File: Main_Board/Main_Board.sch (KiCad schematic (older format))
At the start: 2 parts

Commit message: Started Main Board
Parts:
- added D?: D_Zener, symbol Device:D_Zener
- added J?: 12V_REG_IN, symbol Connector:Screw_Terminal_01x02
- added J?: 12V_REG_OUT, symbol Connector:Screw_Terminal_01x02
- added J?: Conn_02x08_Row_Letter_First, symbol Connector_Generic:Conn_02x08_Row_Letter_First
- added J?: BATT_IN, AMASS_XT60-M, symbol XT60-M:XT60-M
- added Q?: Q_PMOS_GDS, symbol Device:Q_PMOS_GDS
- added R?: R, symbol Device:R
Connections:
- net GND: now also J?.1 (-), J?.2 (Pin_2), J?.2 (Pin_2), R?.2
- net at U?.10 (CS1): no longer U?.10 (CS1)
- net at U?.11 (MOSI): no longer U?.11 (MOSI)
- net at U?.12 (MISO): no longer U?.12 (MISO)
- net at U?.13 (SCK): no longer U?.13 (SCK)
- new net: D?.1 (K), Q?.1 (G), R?.1
- new net: D?.2 (A), J?.1 (Pin_1), Q?.3 (S)
- new net +12V: J?.1 (Pin_1)
- new net +VDC: J?.2 (+), Q?.2 (D)
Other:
- moved on the sheet: U?

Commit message: Rounding up main and light board
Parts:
- removed J?: Conn_02x08_Row_Letter_First, symbol Connector_Generic:Conn_02x08_Row_Letter_First
- added C?: 0.1u, symbol Device:C
- added C?: 47u, symbol Device:C
- added C?: 10n, symbol Device:C_Small
- added C?: 6.8n, symbol Device:C_Small
- added C?: 22u, symbol Device:C
- added J?: Conn_02x07_Counter_Clockwise, symbol Connector_Generic:Conn_02x07_Counter_Clockwise
- added L?: 8.2u, symbol Device:L
- added Q?: Q_PMOS_GDS, symbol Device:Q_PMOS_GDS
- added R?: 100k, symbol Device:R
- added R?: 45.3k, symbol Device:R_Small
- added R? (x2): 10k, symbol Device:R_Small
- added R?: 6.8k, symbol Device:R_Small
- added U?: AP6503, symbol Regulator_Switching:AP6503
- J3: renamed from J?; footprint AMASS_XT60-M -> (none)
- U1, U2: renamed from U?; footprint MODULE_DEV-16771 -> Main_Board:TEENSY_4_1_FP
- gave numbers to parts that had none: 5
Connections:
- net +5V: now also U1.VIN, U2.VIN, C?.1, J?.1 (Pin_1), J?.2 (Pin_2), L?.2, R?.1; no longer U1.5V, U2.5V
- net +VDC: now also C?.1, Q?.3 (S), R?.1, U?.2 (IN); no longer J3.2 (+)
- net GND: now also C?.2, C?.2, C?.2, C?.2, J?.8 (Pin_8), J?.9 (Pin_9), R?.2, R?.2, U?.4 (GND), U?.9 (EP)
- net +3V3: now reaches U1.3.3V_1 (3.3V), U1.3.3V_2 (3.3V), U1.3.3V_3 (3.3V)
- new net: J3.2 (+), Q?.2 (D)
- new net: C?.1, U?.1 (BST)
- new net: C?.2, L?.1, U?.3 (SW)
- new net: R?.1, R?.2, U?.5 (FB)
- new net: R?.1, U?.6 (COMP)
- new net: R?.2, U?.7 (EN)
- new net: C?.1, U?.8 (SS)
- new net: C?.1, R?.2
- new net: Q?.1 (G), R?.1
- new net D: J?.13 (Pin_13)
- new net LIGHT_EN: J?.14 (Pin_14)
- new net P0: J?.3 (Pin_3)
- new net P1: J?.4 (Pin_4)
- new net P2: J?.5 (Pin_5)
- new net P3: J?.6 (Pin_6)
- new net P4: J?.7 (Pin_7)
- new net ~CS: J?.10 (Pin_10)
- new net ~EN: J?.12 (Pin_12)
- new net ~WR: J?.11 (Pin_11)
- no-connect marks 0 -> 2
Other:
- moved on the sheet: D1, J1, J2, J3, Q1, R1

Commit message: Stuff with light
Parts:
- J1: value 12V_REG_IN -> 12V_REG_OUT
- J2: value 12V_REG_OUT -> 12V_REG_IN
- U1: value TEENSY_4_1 -> TEENSY_4_1_MASTER
- U2: value TEENSY_4_1 -> TEENSY_4_1_SLAVE
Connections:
- net +12V: now also Q1.2 (D); no longer J2.1 (Pin_1)
- net +VDC: now also J2.1 (Pin_1); no longer Q1.2 (D)
- net at U1.10 (CS1): now also U2.10 (CS1)
- net at U1.11 (MOSI): now also U2.11 (MOSI)
- net at U1.12 (MISO): now also U2.12 (MISO)
- net SCK_MASTER: now reaches U1.13 (SCK)
- net SCK_MASTER: now also U2.13 (SCK)
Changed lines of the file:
@@
 $EndDescr
-$Comp
-L TEENSY_4_1:TEENSY_4_1 U2
-U 1 1 61B38CB8
-P 12550 7750
-F 0 "U2" H 12550 9917 50  0000 C CNN
-F 1 "TEENSY_4_1" H 12550 9826 50  0000 C CNN
-F 2 "Main_Board:TEENSY_4_1_FP" H 12550 7750 50  0001 L BNN
-F 3 "" H 12550 7750 50  0001 L BNN
-F 4 "Manufacturer recommendations" H 12550 7750 50  0001 L BNN "STANDARD"
-F 5 "4.07mm" H 12550 7750 50  0001 L BNN "MAXIMUM_PACKAGE_HEIGHT"
-F 6 "4.1" H 12550 7750 50  0001 L BNN "PARTREV"
-F 7 "SparkFun Electronics" H 12550 7750 50  0001 L BNN "MANUFACTURER"
-	1    12550 7750
-	-1   0    0    -1
-$EndComp
 $Comp
 L power:GND #PWR0101
@@
 P 10500 7750
 F 0 "U1" H 10500 9917 50  0000 C CNN
-F 1 "TEENSY_4_1" H 10500 9826 50  0000 C CNN
+F 1 "TEENSY_4_1_MASTER" H 10500 9826 50  0000 C CNN
 F 2 "Main_Board:TEENSY_4_1_FP" H 10500 7750 50  0001 L BNN
 F 3 "" H 10500 7750 50  0001 L BNN
@@
 L power:+VDC #PWR0103
 U 1 1 61C63404
-P 16400 6200
-F 0 "#PWR0103" H 16400 6100 50  0001 C CNN
-F 1 "+VDC" H 16400 6475 50  0000 C CNN
-F 2 "" H 16400 6200 50  0001 C CNN
-F 3 "" H 16400 6200 50  0001 C CNN
-	1    16400 6200
+P 17150 7200
+F 0 "#PWR0103" H 17150 7100 50  0001 C CNN
+F 1 "+VDC" H 17150 7475 50  0000 C CNN
+F 2 "" H 17150 7200 50  0001 C CNN
+F 3 "" H 17150 7200 50  0001 C CNN
+	1    17150 7200
 	1    0    0    -1
 $EndComp
@@
 P 16650 7250
 F 0 "J1" H 16600 6950 50  0000 L CNN
-F 1 "12V_REG_IN" H 16450 7050 50  0000 L CNN
+F 1 "12V_REG_OUT" H 16450 7050 50  0000 L CNN
 F 2 "" H 16650 7250 50  0001 C CNN
 F 3 "~" H 16650 7250 50  0001 C CNN
@@
 P 16900 7250
 F 0 "J2" H 16900 7450 50  0000 C CNN
-F 1 "12V_REG_OUT" H 16950 7350 50  0000 C CNN
+F 1 "12V_REG_IN" H 16950 7350 50  0000 C CNN
 F 2 "" H 16900 7250 50  0001 C CNN
 F 3 "~" H 16900 7250 50  0001 C CNN
@@
 L power:+12V #PWR0106
 U 1 1 61C6E3B5
-P 17150 7200
-F 0 "#PWR0106" H 17150 7050 50  0001 C CNN
-F 1 "+12V" H 17165 7373 50  0000 C CNN
-F 2 "" H 17150 7200 50  0001 C CNN
-F 3 "" H 17150 7200 50  0001 C CNN
-	1    17150 7200
+P 16400 6200
+F 0 "#PWR0106" H 16400 6050 50  0001 C CNN
+F 1 "+12V" H 16415 6373 50  0000 C CNN
+F 2 "" H 16400 6200 50  0001 C CNN
+F 3 "" H 16400 6200 50  0001 C CNN
+	1    16400 6200
 	1    0    0    -1
 $EndComp
@@
 Wire Wire Line
 	20050 9050 19950 9050
+Wire Wire Line
+	11300 8150 11750 8150
+Wire Wire Line
+	11300 8250 11750 8250
+Wire Wire Line
+	11300 7950 11750 7950
+$Comp
+L TEENSY_4_1:TEENSY_4_1 U2
+U 1 1 61B38CB8
+P 12550 7750
+F 0 "U2" H 12550 9917 50  0000 C CNN
+F 1 "TEENSY_4_1_SLAVE" H 12550 9826 50  0000 C CNN
+F 2 "Main_Board:TEENSY_4_1_FP" H 12550 7750 50  0001 L BNN
+F 3 "" H 12550 7750 50  0001 L BNN
+F 4 "Manufacturer recommendations" H 12550 7750 50  0001 L BNN "STANDARD"
+F 5 "4.07mm" H 12550 7750 50  0001 L BNN "MAXIMUM_PACKAGE_HEIGHT"
+F 6 "4.1" H 12550 7750 50  0001 L BNN "PARTREV"
+F 7 "SparkFun Electronics" H 12550 7750 50  0001 L BNN "MANUFACTURER"
+	1    12550 7750
+	-1   0    0    -1
+$EndComp
+Text GLabel 9600 8350 0    50   Output ~ 0
+SCK_MASTER
+Wire Wire Line
+	9600 8350 9700 8350
+Text GLabel 13500 8350 2    50   Input ~ 0
+SCK_MASTER
+Wire Wire Line
+	13500 8350 13350 8350
+$Comp
+L Graphic:SYM_Arrow_Small #SYM?
+U 1 1 61E13D0E
+P 11500 8250
+F 0 "#SYM?" H 11500 8310 50  0001 C CNN
+F 1 "SYM_Arrow_Small" H 11510 8200 50  0001 C CNN
+F 2 "" H 11500 8250 50  0001 C CNN
+F 3 "~" H 11500 8250 50  0001 C CNN
+	1    11500 8250
+	1    0    0    -1
+$EndComp
+$Comp
+L Graphic:SYM_Arrow_Small #SYM?
+U 1 1 61E15938
+P 11500 8150
+F 0 "#SYM?" H 11500 8210 50  0001 C CNN
+F 1 "SYM_Arrow_Small" H 11510 8100 50  0001 C CNN
+F 2 "" H 11500 8150 50  0001 C CNN
+F 3 "~" H 11500 8150 50  0001 C CNN
+	1    11500 8150
+	-1   0    0    1
+$EndComp
+$Comp
+L Graphic:SYM_Arrow_Small #SYM?
+U 1 1 61E1785A
+P 11500 7950
+F 0 "#SYM?" H 11500 8010 50  0001 C CNN
+F 1 "SYM_Arrow_Small" H 11510 7900 50  0001 C CNN
+F 2 "" H 11500 7950 50  0001 C CNN
+F 3 "~" H 11500 7950 50  0001 C CNN
+	1    11500 7950
+	1    0    0    -1
+$EndComp
 $EndSCHEMATC

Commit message: motor drivers added
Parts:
- added D? (x4): WS2812B, LED_SMD:LED_WS2812B_PLCC4_5.0x5.0mm_P3.2mm, symbol LED:WS2812B
- added J?: Conn_02x08_Row_Letter_First, symbol Connector_Generic:Conn_02x08_Row_Letter_First
- added R?: 10k, symbol Device:R
- added SW?: SW_Push, symbol Switch:SW_Push
- added SW?: SW_SPST, symbol Switch:SW_SPST
- added U? (x3): G2-24v13, symbol Main_Board:G2-24v13
- R1: value R -> 10k
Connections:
- net +3V3: now also J?.b1 (Pin_b1), SW?.2
- net +5V: now also D?.1 (VDD), D?.1 (VDD), D?.1 (VDD), D?.1 (VDD)
- net GND: now also D?.3 (VSS), D?.3 (VSS), D?.3 (VSS), D?.3 (VSS), J?.a1 (Pin_a1), R?.1, SW?.1 (A); no longer R?.2
- new net: R?.2, SW?.2 (B)
- new net: D?.2 (DOUT), D?.4 (DIN) (x4)
- new net HOLD_SW: R?.2, SW?.1
- new net IR1: J?.a8 (Pin_a8)
- new net IR10: J?.b6 (Pin_b6)
- new net IR11: J?.b5 (Pin_b5)
- new net IR12: J?.b4 (Pin_b4)
- new net IR13: J?.b3 (Pin_b3)
- new net IR14: J?.b2 (Pin_b2)
- new net IR2: J?.a7 (Pin_a7)
- new net IR3: J?.a6 (Pin_a6)
- new net IR4: J?.a5 (Pin_a5)
- new net IR5: J?.a4 (Pin_a4)
- new net IR6: J?.a3 (Pin_a3)
- new net IR7: J?.a2 (Pin_a2)
- new net IR8: J?.b8 (Pin_b8)
- new net IR9: J?.b7 (Pin_b7)
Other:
- moved on the sheet: C?, D1, J1, J2, J3, L?, Q1, Q?, R1, R?, U?

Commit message: changed document settings
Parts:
- added J? (x3): Conn_01x06, symbol Connector_Generic:Conn_01x06
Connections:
- net +12V: now also U?.4 (VIN), U?.4 (VIN), U?.4 (VIN)
- net GND: now also U?.1 (GND), U?.1 (GND), U?.1 (GND)
- net at U?.2 (OUTB): now also J?.1 (Pin_1) (x3)
- net at U?.3 (OUTA): now also J?.2 (Pin_2) (x3)
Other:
- moved on the sheet: C?, D1, D?, J1, J2, J3, J?, L?, Q1, Q?, R1, R?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

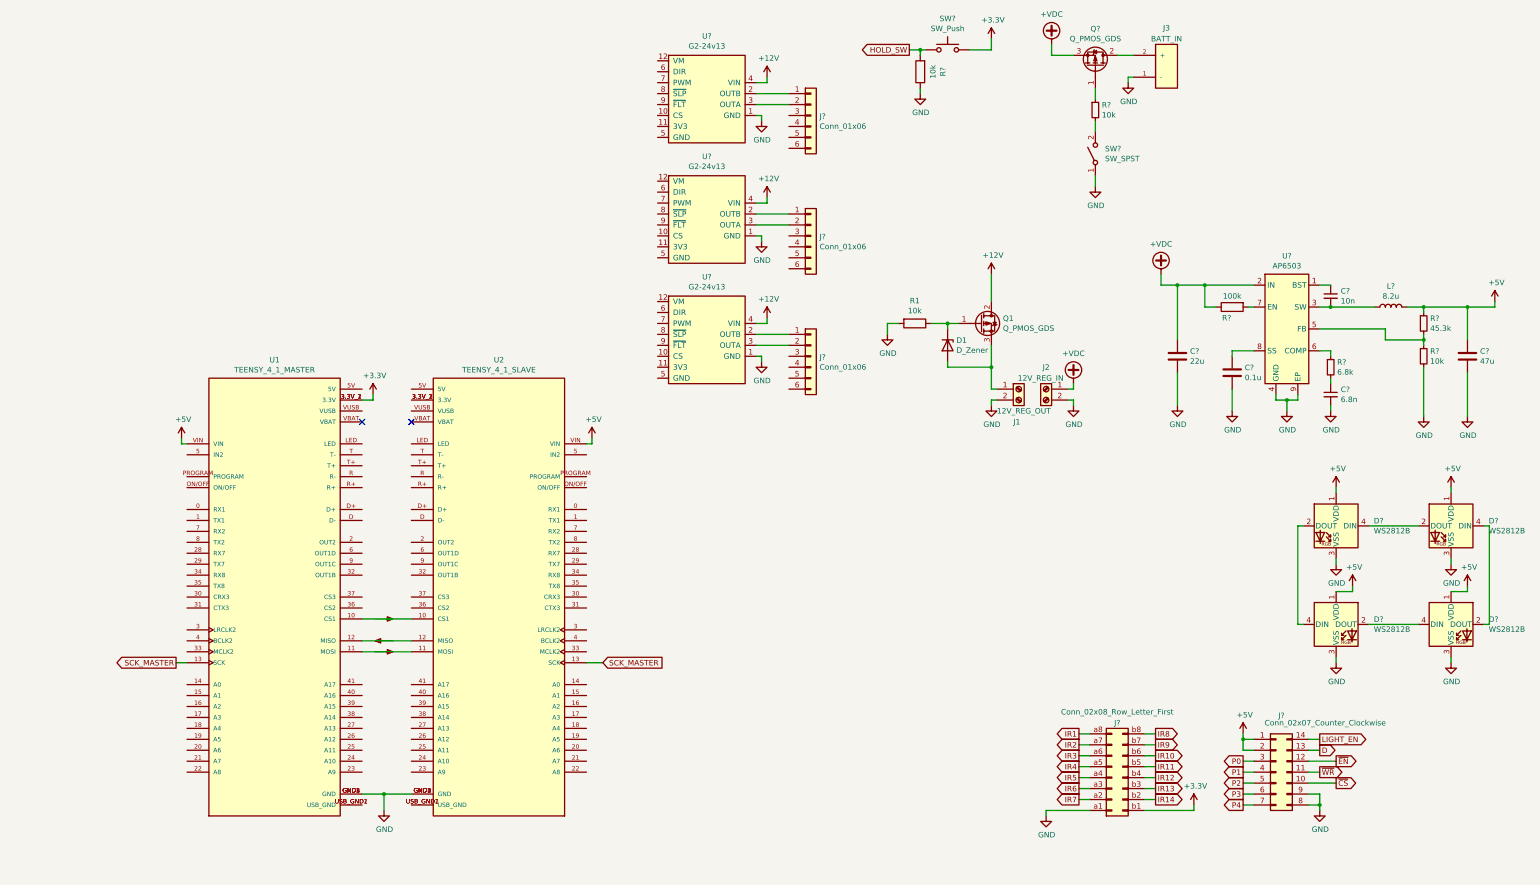
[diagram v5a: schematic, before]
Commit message: Added all connectors, layout for pins
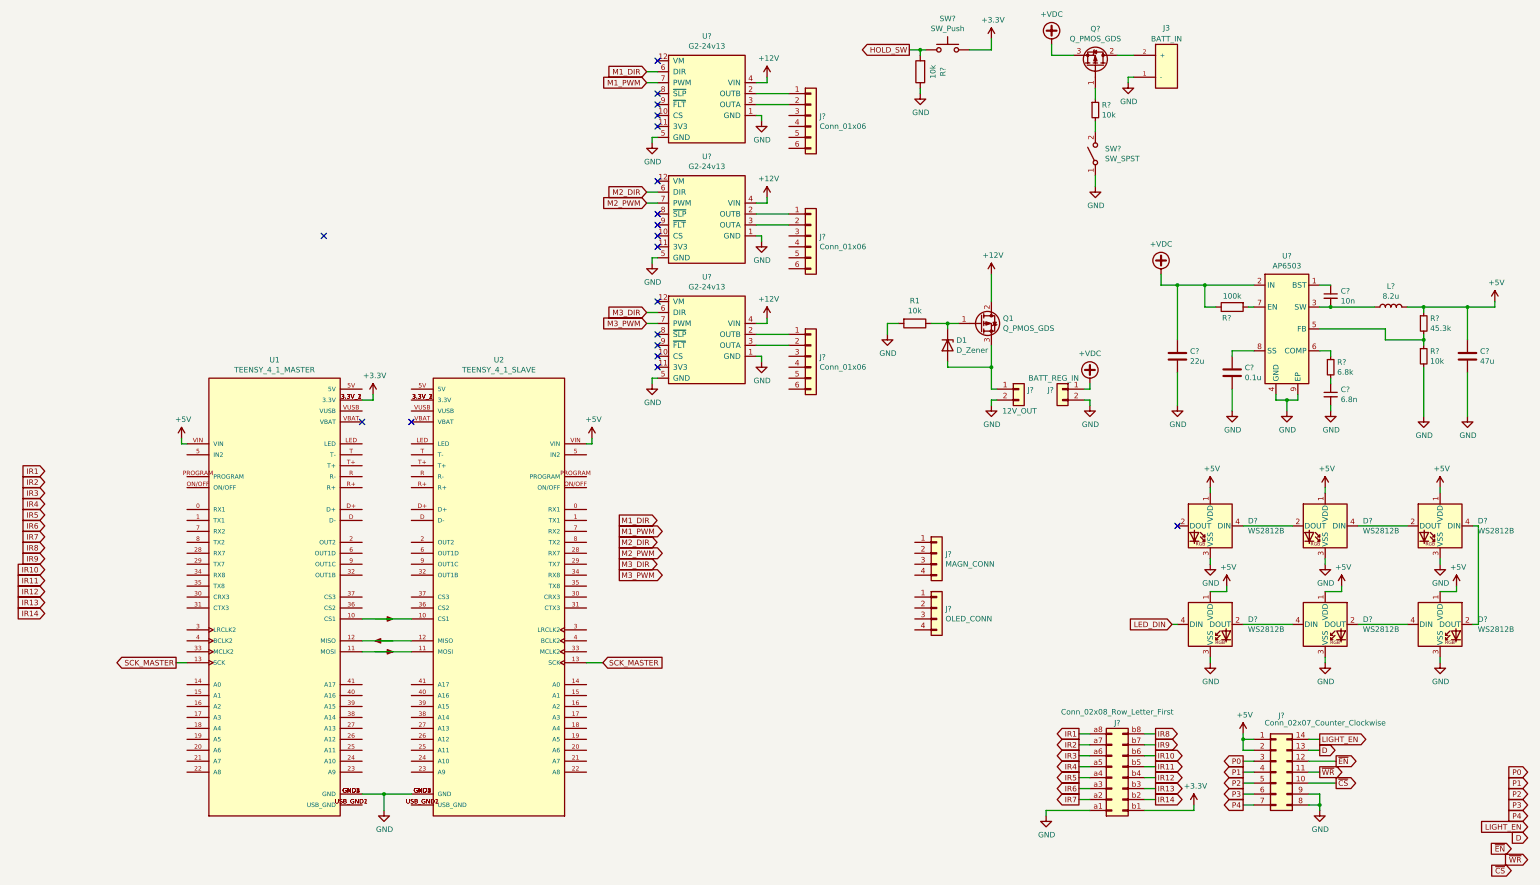
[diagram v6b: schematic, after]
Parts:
- removed J1: 12V_REG_OUT, symbol Connector:Screw_Terminal_01x02
- removed J2: 12V_REG_IN, symbol Connector:Screw_Terminal_01x02
- added D? (x2): WS2812B, LED_SMD:LED_WS2812B_PLCC4_5.0x5.0mm_P3.2mm, symbol LED:WS2812B
- added J?: MAGN_CONN, symbol Connector_Generic:Conn_01x04
- added J?: OLED_CONN, symbol Connector_Generic:Conn_01x04
- added J?: 12V_OUT, symbol Connector_Generic:Conn_01x02
- added J?: BATT_REG_IN, symbol Connector_Generic:Conn_01x02
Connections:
- net +5V: now also D?.1 (VDD), D?.1 (VDD)
- net +VDC: now also J?.1 (Pin_1)
- net GND: now also U?.5 (GND), U?.5 (GND), U?.5 (GND), D?.3 (VSS), D?.3 (VSS), J?.2 (Pin_2), J?.2 (Pin_2)
- net at D1.2 (A), Q1.3 (S): now also J?.1 (Pin_1)
- net at D?.2 (DOUT): no longer D?.4 (DIN)
- net at D?.4 (DIN): now also D?.2 (DOUT); no longer D?.2 (DOUT) (x2)
- net M1_DIR: now reaches U?.6 (DIR)
- net M1_PWM: now reaches U?.7 (PWM)
- net M2_DIR: now reaches U?.6 (DIR)
- net M2_PWM: now reaches U?.7 (PWM)
- net M3_DIR: now reaches U?.6 (DIR)
- net M3_PWM: now reaches U?.7 (PWM)
- new net: D?.2 (DOUT), D?.4 (DIN) (x2)
- new net LED_DIN: D?.4 (DIN)
- no-connect marks 2 -> 19
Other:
- moved on the sheet: D?

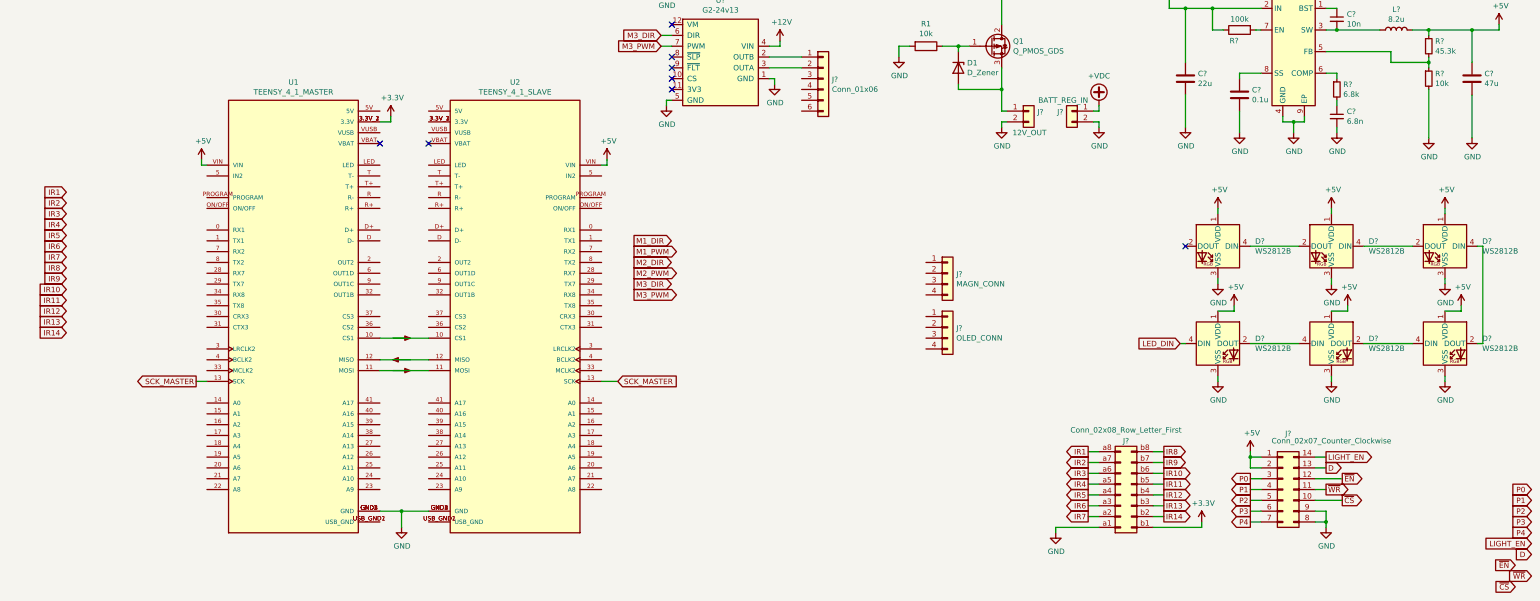
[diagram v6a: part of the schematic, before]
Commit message: Started connecting main board
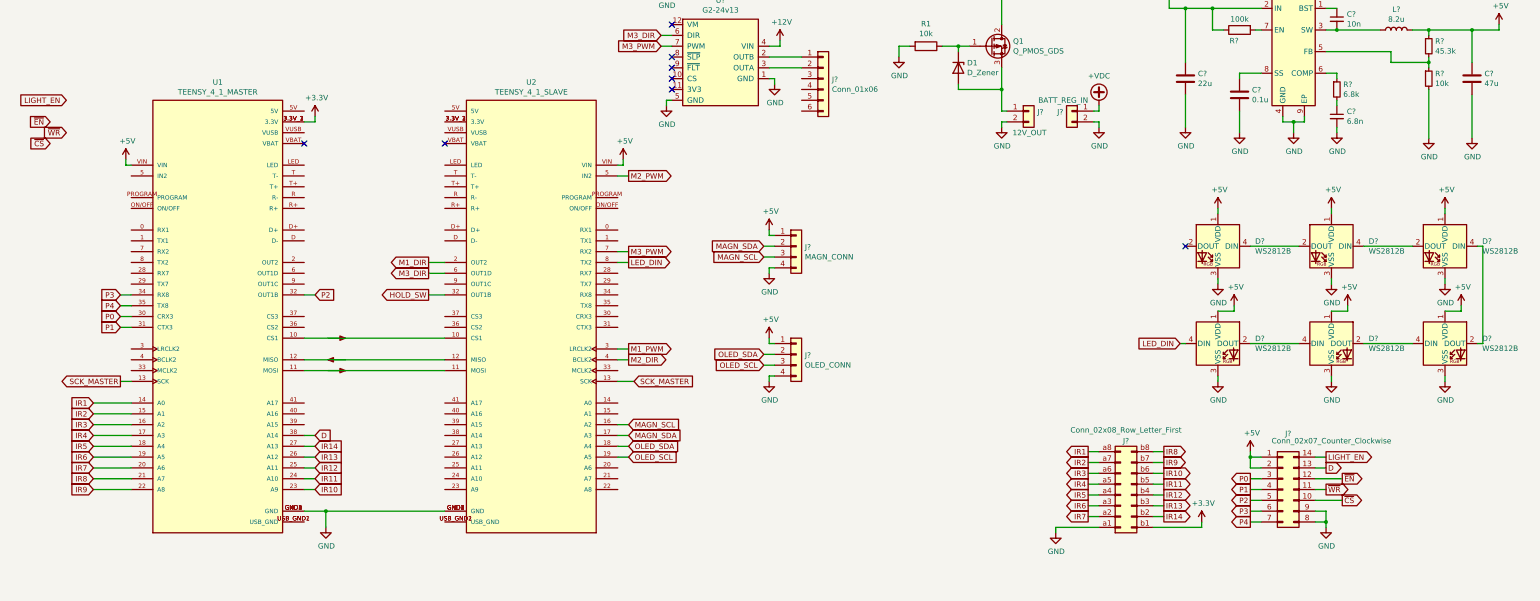
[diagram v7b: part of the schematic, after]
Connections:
- net +5V: now also J?.1 (Pin_1), J?.1 (Pin_1)
- net D: now also U1.38 (A14)
- net GND: now also J?.4 (Pin_4), J?.4 (Pin_4)
- net HOLD_SW: now also U2.32 (OUT1B)
- net IR1: now also U1.14 (A0)
- net IR10: now also U1.23 (A9)
- net IR11: now also U1.24 (A10)
- net IR12: now also U1.25 (A11)
- net IR13: now also U1.26 (A12)
- net IR14: now also U1.27 (A13)
- net IR2: now also U1.15 (A1)
- net IR3: now also U1.16 (A2)
- net IR4: now also U1.17 (A3)
- net IR5: now also U1.18 (A4)
- net IR6: now also U1.19 (A5)
- net IR7: now also U1.20 (A6)
- net IR8: now also U1.21 (A7)
- net IR9: now also U1.22 (A8)
- net LED_DIN: now also U2.8 (TX2)
- net M1_DIR: now also U2.2 (OUT2)
- net M1_PWM: now also U2.3 (LRCLK2)
- net M2_DIR: now also U2.4 (BCLK2)
- net M2_PWM: now also U2.5 (IN2)
- net M3_DIR: now also U2.6 (OUT1D)
- net M3_PWM: now also U2.7 (RX2)
- net P0: now also U1.30 (CRX3)
- net P1: now also U1.31 (CTX3)
- net P2: now also U1.32 (OUT1B)
- net P3: now also U1.34 (RX8)
- net P4: now also U1.35 (TX8)
- net MAGN_SCL: now reaches U2.16 (A2)
- net MAGN_SCL: now also J?.3 (Pin_3)
- net MAGN_SDA: now reaches U2.17 (A3)
- net MAGN_SDA: now also J?.2 (Pin_2)
- net OLED_SDA: now reaches U2.18 (A4)
- net OLED_SDA: now also J?.2 (Pin_2)
- net OLED_SCL: now reaches U2.19 (A5)
- net OLED_SCL: now also J?.3 (Pin_3)
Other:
- moved on the sheet: J?, U1, U2

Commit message: started buck CC driver for LPCB
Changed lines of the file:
@@
 L Graphic:SYM_Arrow_Small #SYM?
 U 1 1 61E13D0E
-P 4500 7450
-F 0 "#SYM?" H 4500 7510 50  0001 C CNN
-F 1 "SYM_Arrow_Small" H 4510 7400 50  0001 C CNN
-F 2 "" H 4500 7450 50  0001 C CNN
-F 3 "~" H 4500 7450 50  0001 C CNN
-	1    4500 7450
+P 4850 7450
+F 0 "#SYM?" H 4850 7510 50  0001 C CNN
+F 1 "SYM_Arrow_Small" H 4860 7400 50  0001 C CNN
+F 2 "" H 4850 7450 50  0001 C CNN
+F 3 "~" H 4850 7450 50  0001 C CNN
+	1    4850 7450
 	1    0    0    -1
 $EndComp
@@
 L Graphic:SYM_Arrow_Small #SYM?
 U 1 1 61E15938
-P 4500 7350
-F 0 "#SYM?" H 4500 7410 50  0001 C CNN
-F 1 "SYM_Arrow_Small" H 4510 7300 50  0001 C CNN
-F 2 "" H 4500 7350 50  0001 C CNN
-F 3 "~" H 4500 7350 50  0001 C CNN
-	1    4500 7350
+P 4850 7350
+F 0 "#SYM?" H 4850 7410 50  0001 C CNN
+F 1 "SYM_Arrow_Small" H 4860 7300 50  0001 C CNN
+F 2 "" H 4850 7350 50  0001 C CNN
+F 3 "~" H 4850 7350 50  0001 C CNN
+	1    4850 7350
 	-1   0    0    1
 $EndComp
@@
 L Graphic:SYM_Arrow_Small #SYM?
 U 1 1 61E1785A
-P 4500 7150
-F 0 "#SYM?" H 4500 7210 50  0001 C CNN
-F 1 "SYM_Arrow_Small" H 4510 7100 50  0001 C CNN
-F 2 "" H 4500 7150 50  0001 C CNN
-F 3 "~" H 4500 7150 50  0001 C CNN
-	1    4500 7150
+P 4850 7150
+F 0 "#SYM?" H 4850 7210 50  0001 C CNN
+F 1 "SYM_Arrow_Small" H 4860 7100 50  0001 C CNN
+F 2 "" H 4850 7150 50  0001 C CNN
+F 3 "~" H 4850 7150 50  0001 C CNN
+	1    4850 7150
 	1    0    0    -1
 $EndComp
@@
 F 3 "~" H 9000 3650 50  0001 C CNN
 	1    9000 3650
-	1    0    0    -1
-$EndComp
-$Comp
-L Connector_Generic:Conn_01x06 J?
-U 1 1 61ECCE02
-P 9000 4750
-F 0 "J?" H 9080 4742 50  0000 L CNN
-F 1 "Conn_01x06" H 9080 4651 50  0000 L CNN
-F 2 "" H 9000 4750 50  0001 C CNN
-F 3 "~" H 9000 4750 50  0001 C CNN
-	1    9000 4750
 	1    0    0    -1
 $EndComp
@@
 Wire Wire Line
 	7200 8250 7100 8250
+$Comp
+L Connector_Generic:Conn_01x06 J?
+U 1 1 61ECCE02
+P 9000 4750
+F 0 "J?" H 9080 4742 50  0000 L CNN
+F 1 "Conn_01x06" H 9080 4651 50  0000 L CNN
+F 2 "" H 9000 4750 50  0001 C CNN
+F 3 "~" H 9000 4750 50  0001 C CNN
+	1    9000 4750
+	1    0    0    -1
+$EndComp
 $EndSCHEMATC
